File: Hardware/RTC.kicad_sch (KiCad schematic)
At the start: 15 parts, among them IC1 RTC_DS3231M, U8 PCF8563TS, Y2 MC-306

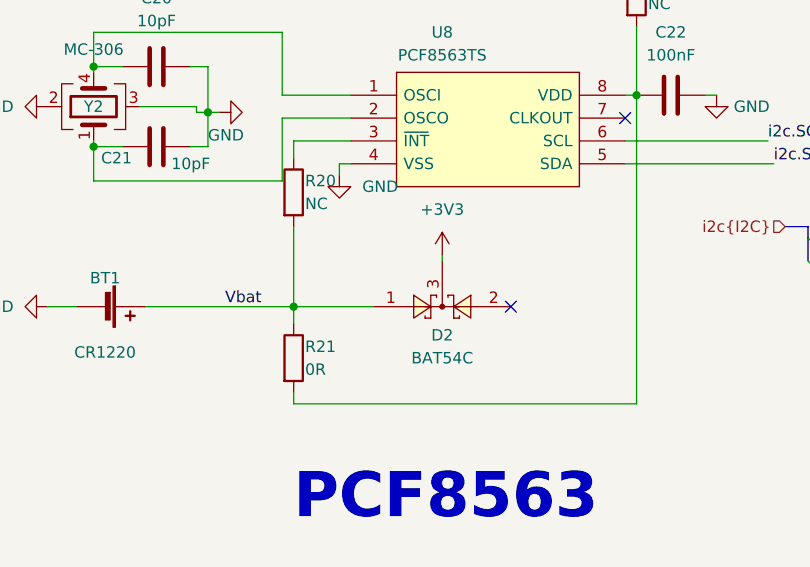
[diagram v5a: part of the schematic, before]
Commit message: complete PCB & fix SCH
fix pull push resistor Pin A, B RS485
diode RTC PCF8564
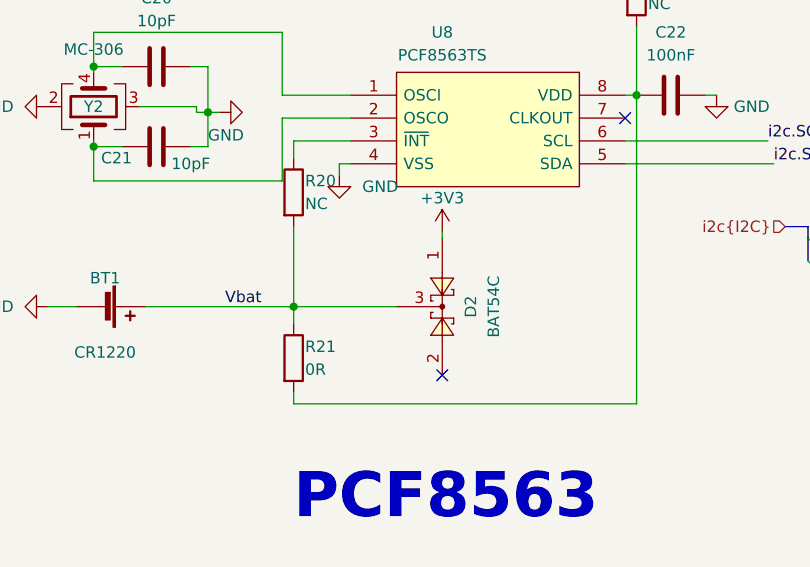
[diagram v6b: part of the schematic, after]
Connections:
- net +3V3: now also D2.1; no longer D2.3
- net Vbat: now also D2.3; no longer D2.1
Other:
- moved on the sheet: D2
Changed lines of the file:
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@@
   (no_connect (at 231.14 60.96))
   (no_connect (at 116.84 52.705))
-  (no_connect (at 104.14 73.66))
+  (no_connect (at 96.52 81.28))
   (no_connect (at 205.74 71.12))
   (no_connect (at 231.14 71.12))
@@
     (stroke (width 0) (type default))
   )
-  (wire (pts (xy 80.01 73.66) (xy 88.9 73.66))
-    (stroke (width 0) (type default))
-  )
   (wire (pts (xy 116.84 50.165) (xy 118.11 50.165))
     (stroke (width 0) (type default))
   )
-  (wire (pts (xy 80.01 75.565) (xy 80.01 73.66))
+  (wire (pts (xy 80.01 73.66) (xy 80.01 75.565))
     (stroke (width 0) (type default))
   )
@@
     (stroke (width 0) (type default))
   )
-  (wire (pts (xy 96.52 68.58) (xy 96.52 67.945))
+  (wire (pts (xy 96.52 65.405) (xy 96.52 66.04))
     (stroke (width 0) (type default))
   )
@@
   )
   (wire (pts (xy 201.93 46.99) (xy 201.93 52.07))
+    (stroke (width 0) (type default))
+  )
+  (wire (pts (xy 91.44 73.66) (xy 80.01 73.66))
     (stroke (width 0) (type default))
   )
@@
     )
   )
-  (symbol (lib_id "IVS_SYMBOLS:BAT54C") (at 96.52 73.66 0) (mirror x) (unit 1)
+  (symbol (lib_id "IVS_SYMBOLS:BAT54C") (at 96.52 73.66 270) (unit 1)
     (in_bom yes) (on_board yes) (dnp no)
-    (property "Reference" "D2" (at 96.52 76.835 0)
-      (effects (font (size 1.27 1.27)))
-    )
-    (property "Value" "BAT54C" (at 96.52 79.375 0)
+    (property "Reference" "D2" (at 99.695 73.66 0)
+      (effects (font (size 1.27 1.27)))
+    )
+    (property "Value" "BAT54C" (at 102.235 73.66 0)
       (effects (font (size 1.27 1.27)))
     )
@@
       (effects (font (size 1.27 1.27)) (justify left) hide)
     )
-    (property "Datasheet" "http://www.diodes.com/_files/datasheets/ds11005.pdf" (at 96.52 58.42 0)
+    (property "Datasheet" "http://www.diodes.com/_files/datasheets/ds11005.pdf" (at 81.28 73.66 0)
       (effects (font (size 1.27 1.27)) hide)
     )
@@
     )
   )
-  (symbol (lib_id "power:+3V3") (at 96.52 67.945 0) (unit 1)
-    (in_bom yes) (on_board yes) (dnp no) (fields_autoplaced)
-    (property "Reference" "#PWR054" (at 96.52 71.755 0)
-      (effects (font (size 1.27 1.27)) hide)
-    )
-    (property "Value" "+3V3" (at 96.52 62.865 0)
-      (effects (font (size 1.27 1.27)))
-    )
-    (property "Footprint" "" (at 96.52 67.945 0)
-      (effects (font (size 1.27 1.27)) hide)
-    )
-    (property "Datasheet" "" (at 96.52 67.945 0)
-      (effects (font (size 1.27 1.27)) hide)
-    )
+  (symbol (lib_id "power:+3V3") (at 96.52 65.405 0) (unit 1)
+    (in_bom yes) (on_board yes) (dnp no)
+    (property "Reference" "#PWR054" (at 96.52 69.215 0)
+      (effects (font (size 1.27 1.27)) hide)
+    )
+    (property "Value" "+3V3" (at 96.52 61.595 0)
+      (effects (font (size 1.27 1.27)))
+    )
+    (property "Footprint" "" (at 96.52 65.405 0)
+      (effects (font (size 1.27 1.27)) hide)
+    )
+    (property "Datasheet" "" (at 96.52 65.405 0)
+      (effects (font (size 1.27 1.27)) hide)
+    )

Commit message: add lora, relay, opto, opamp block, led for 74595. Delete RT9193, connect boot0,1 to GND. Fix footprint crystal 8M, 74HC595, IDC pin
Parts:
- removed Y2: MC-306, Crystal:Crystal_SMD_SeikoEpson_MC306-4Pin_8.0x3.2mm, symbol Device:Crystal_GND23
- added Y2: 32.768kHz, IVS_FOOTPRINTS:Crystal_MC306, symbol IVS_SYMBOLS:Crystal_RTC
- C20, C21, C22, C23, C24: footprint IVS_FOOTPRINTS:C0603 -> IVS_FOOTPRINTS:C_0603
- IC1: footprint Package_SO:SOIC-16W_7.5x10.3mm_P1.27mm -> IVS_FOOTPRINTS:SOIC-16W_7.5x10.3mm_P1.27mm
- R20, R21, R22, R42: footprint IVS_FOOTPRINTS:R0603 -> IVS_FOOTPRINTS:R_0603
- U8: footprint IVS_FOOTPRINTS:SOIC-8 -> IVS_FOOTPRINTS:SOIC-8_3.9x4.9mm_P1.27mm
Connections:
- net GND: now also Y2.2, Y2.3
- net at C21.1, U8.2 (OSCO): now also Y2.4
- net at C20.1, U8.1 (OSCI): now also Y2.1
